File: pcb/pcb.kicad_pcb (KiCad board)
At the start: 2 copper layers, 152 x 91.6 mm, 66 parts, among them J1 USB_C_Receptacle_USB2.0_16P, J2 Conn_01x02, K1 SW_Push, K10 SW_Push, K11 SW_Push, K12 SW_Push, K13 SW_Push, K14 SW_Push, K15 SW_Push, K16 SW_Push, K17 SW_Push, K18 SW_Push, K19 SW_Push, K2 SW_Push, K20 SW_Push, K21 SW_Push, K3 SW_Push, K4 SW_Push, K5 SW_Push, K6 SW_Push, K7 SW_Push, K8 SW_Push, K9 SW_Push, U1 SRV05-4, U2 ProMicro, U3 SRV05-4

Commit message: cirrus40, second manufactured version
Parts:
- removed the D19 at (50.2, 74.3)
- removed the D20 at (63.5, 93.3)
- removed D22: DIODE, footprints:Diode-dual
- removed K19, K20, K21: SW_Push, footprints:SW_MX_HotSwap_Reversible
- removed the REF** at (97.5, 61.3)
- added C1: 470nF, Capacitor_SMD:C_0805_2012Metric_Pad1.18x1.45mm_HandSolder, B.Cu at (154.9, 94.0)
- added C3: 470nF, Capacitor_SMD:C_0805_2012Metric_Pad1.18x1.45mm_HandSolder, B.Cu at (159.4, 94.0)
- added D12: DIODE, footprints:Diode-dual, F.Cu at (158.1, 100.3)
- added D21: DIODE, footprints:Diode-dual, F.Cu at (160.7, 100.3)
- added R1: 10kOhm, Resistor_SMD:R_0805_2012Metric_Pad1.20x1.40mm_HandSolder, F.Cu at (155.6, 102.2)
- added R2: 10kOhm, Resistor_SMD:R_0805_2012Metric_Pad1.20x1.40mm_HandSolder, B.Cu at (155.6, 102.2)
- added R3: 8kOhm, Resistor_SMD:R_0805_2012Metric_Pad1.20x1.40mm_HandSolder, B.Cu at (155.6, 97.8)
- added R4: 8kOhm, Resistor_SMD:R_0805_2012Metric_Pad1.20x1.40mm_HandSolder, F.Cu at (155.6, 97.8)
- added R5: 10kOhm, Resistor_SMD:R_0805_2012Metric_Pad1.20x1.40mm_HandSolder, B.Cu at (163.2, 102.2)
- added R6: 10kOhm, Resistor_SMD:R_0805_2012Metric_Pad1.20x1.40mm_HandSolder, F.Cu at (163.2, 102.2)
- added R7: 8kOhm, Resistor_SMD:R_0805_2012Metric_Pad1.20x1.40mm_HandSolder, F.Cu at (163.2, 97.8)
- added R8: 8kOhm, Resistor_SMD:R_0805_2012Metric_Pad1.20x1.40mm_HandSolder, B.Cu at (163.2, 97.8)
- C2: renamed from C1; value 50V/100nF axial -> 470nF; footprint footprints:RESISTOR_Reversible -> Capacitor_SMD:C_0805_2012Metric_Pad1.18x1.45mm_HandSolder
- C4: renamed from C2; value 50V/100nF axial -> 470nF; footprint footprints:RESISTOR_Reversible -> Capacitor_SMD:C_0805_2012Metric_Pad1.18x1.45mm_HandSolder
- FB1: renamed from FB2; footprint footprints:C_0603_1608Metric_Pad1.08x0.95mm_HandSolder -> Capacitor_SMD:C_0805_2012Metric_Pad1.18x1.45mm_HandSolder
- FB2: renamed from FB3; footprint footprints:C_0603_1608Metric_Pad1.08x0.95mm_HandSolder -> Capacitor_SMD:C_0805_2012Metric_Pad1.18x1.45mm_HandSolder
- FB3: renamed from FB4; footprint footprints:C_0603_1608Metric_Pad1.08x0.95mm_HandSolder -> Capacitor_SMD:C_0805_2012Metric_Pad1.18x1.45mm_HandSolder
- FB4: renamed from FB1; footprint footprints:C_0603_1608Metric_Pad1.08x0.95mm_HandSolder -> Capacitor_SMD:C_0805_2012Metric_Pad1.18x1.45mm_HandSolder
- REF** (x6): value MountingHole_2.2mm_M2 -> MountingHole_3.5mm_TinyCourtyard; footprint MountingHole:MountingHole_2.2mm_M2 -> footprints:MountingHole_3.5mm_TinyCourtyard
- moved REF** 38.1 mm to (135.5, 102.2)
- moved J2 36.3 mm to (166.4, 64.1), turned to -90 degrees
- moved REF** 19.1 mm to (78.5, 65.9)
- moved REF** 19.1 mm to (78.5, 104.2)
- moved D14 17.4 mm to (125.5, 87.5)
- moved FB1 16.5 mm to (165.8, 110.3), turned to -90 degrees
- moved FB2 16.5 mm to (165.8, 110.3), turned to -90 degrees
- moved D2 15.3 mm to (68.6, 92.1)
- moved D10 15.3 mm to (106.5, 88.4)
- moved D5 15.0 mm to (87.6, 87.6)
- moved C2 13.2 mm to (154.9, 94.0), turned to 180 degrees
- moved FB3 12.2 mm to (163.5, 110.3), turned to -90 degrees
- moved FB4 12.2 mm to (163.5, 110.3), turned to -90 degrees
- moved D11 10.4 mm to (129.5, 118.7), turned to 90 degrees
- moved C4 8.63 mm to (159.4, 94.0), turned to 0 degrees
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- renumbered D13 to D1, D9 to D10, D18 to D11, D4 to D13, D5 to D14, D6 to D15, D17 to D16, D1 to D17, D2 to D18, D3 to D19, D14 to D2, D16 to D20, D15 to D3, D10 to D4, D11 to D5, D12 to D6, D21 to D7, D7 to D8, D8 to D9, K13 to K1, K18 to K10, K4 to K11, K5 to K12, K6 to K13, K17 to K14, K1 to K15, K2 to K16, K3 to K17, K16 to K18, K14 to K2, K15 to K3, K10 to K4, K11 to K5, K12 to K6, U3 to U1, U1 to U2, U2 to U3
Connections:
- C2 pad 1: ENCA -> ENCA_DB
- C4 pad 1: GND -> ENCB_DB
- C4 pad 2: ENCB -> GND
- U3 pad 2: ROW0 -> unconnected-(U3-GP2-Pad2)
- U3 pad 20: COL5 -> COL4
- U3 pad 22: COL4 -> COL3
- U3 pad 26: COL3 -> COL2
- U3 pad 27: COL2 -> COL1
- U3 pad 28: COL1 -> COL0
- U3 pad 29: COL0 -> unconnected-(U3-GP29-Pad29)
- U3 pad 3: ROW1 -> ROW0
- U3 pad 4: ROW2 -> ROW1
- U3 pad 5: ROW3 -> ROW2
- U3 pad 6: ENCA -> ROW3
- U3 pad 7: ENCB -> unconnected-(U3-GP7-Pad7)
- U3 pad 8: unconnected-(U2-GP8-Pad8)_1 -> ENCA_DB
- U3 pad 9: unconnected-(U2-GP9-Pad9) -> ENCB_DB
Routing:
- net COL5: track 202.3 -> 0.00 mm, vias 8 -> 0
- net ENCA: track 105.0 -> 58.5 mm, vias 6 -> 1
- net COL4: track 184.2 -> 142.7 mm, vias 6 -> 3
- net ENCB: track 95.8 -> 55.7 mm, vias 5 -> 1
- net /Batt: track 52.1 -> 12.2 mm, vias 2 -> 1
- net ROW1: track 143.1 -> 105.8 mm, vias 4 -> 2
- net ENCA_DB: track 0.00 -> 37.2 mm
- net COL0: track 176.6 -> 141.0 mm, vias 7 -> 4
- net ENCB_DB: track 0.00 -> 34.9 mm
- net Net-(D20-K) (its old number): track 32.6 -> 0.00 mm, vias 2 -> 0
- net ROW3: track 132.5 -> 102.9 mm, vias 3 -> 1
- net ROW2: track 127.8 -> 106.1 mm, vias 1 -> 2
- net ROW0: track 117.4 -> 96.4 mm, vias 0 -> 1
- net VCC: track 75.6 -> 96.4 mm, vias 8 -> 6
- net COL3: track 193.5 -> 174.3 mm, vias 7 -> 4
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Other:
- board size 152 x 91.6 mm -> 133.2 x 91.6 mm

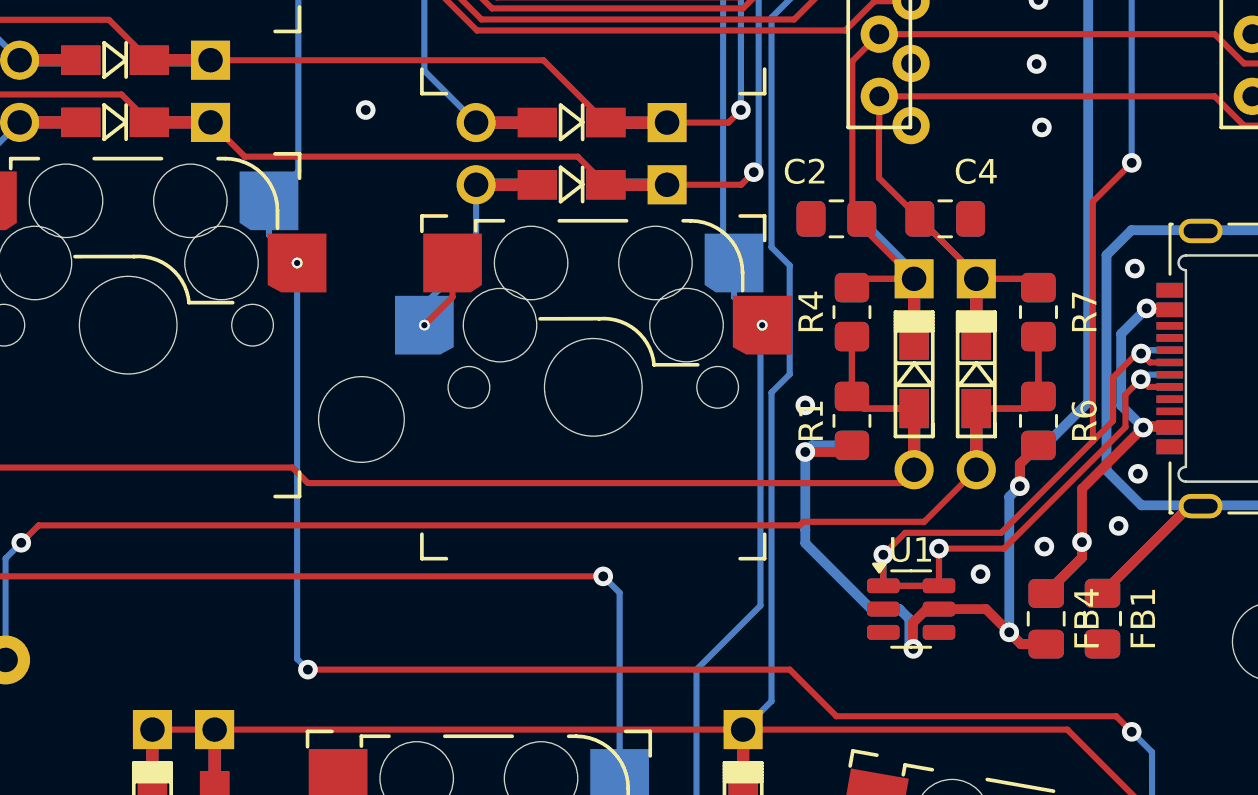
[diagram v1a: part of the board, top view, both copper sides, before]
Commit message: add cap/resistor labels and github link
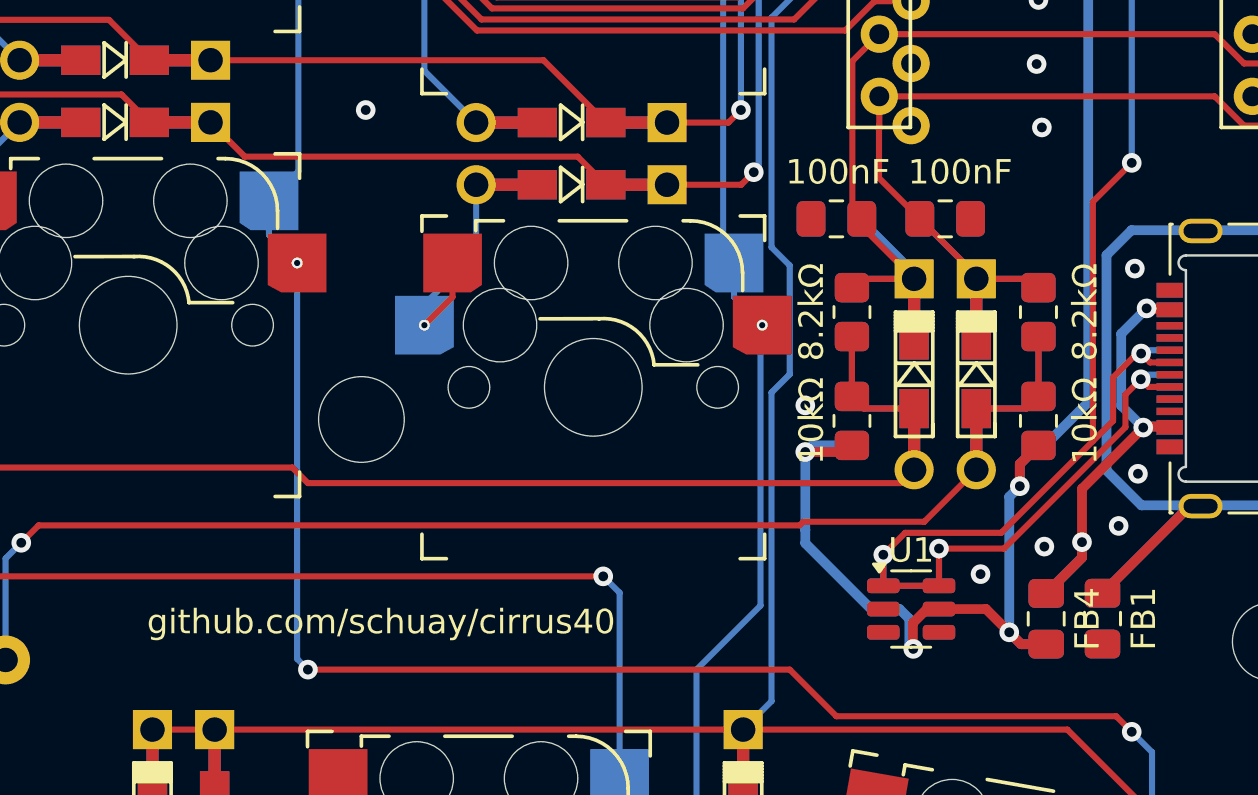
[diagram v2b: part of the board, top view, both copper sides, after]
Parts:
- renumbered C4 to 100nF, C2 to 100nF, C1 to 100nF, C3 to 100nF, R6 to 10kΩ, R1 to 10kΩ, R5 to 10kΩ, R2 to 10kΩ, R7 to 8.2kΩ, R4 to 8.2kΩ, R3 to 8.2kΩ, R8 to 8.2kΩ
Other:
- board text added: "github.com/schuay/cirrus40"
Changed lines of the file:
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@@
 		(descr "Capacitor SMD 0805 (2012 Metric), square (rectangular) end terminal, IPC-7351 nominal with elongated pad for handsoldering. (Body size source: IPC-SM-782 page 76, https://www.pcb-3d.com/wordpress/wp-content/uploads/ipc-sm-782a_amendment_1_and_2.pdf, https://docs.google.com/spreadsheets/d/1BsfQQcO9C6DZCsRaXUlFlo91Tg2WpOkGARC1WS5S8t0/edit?usp=sharing), generated with kicad-footprint-generator")
 		(tags "capacitor handsolder")
-		(property "Reference" "C4"
-			(at 1.27 -1.905 0)
+		(property "Reference" "100nF"
+			(at 0.615 -1.905 0)
 			(layer "F.SilkS")
 			(effects
@@
 		(descr "Resistor SMD 0805 (2012 Metric), square (rectangular) end terminal, IPC-7351 nominal with elongated pad for handsoldering. (Body size source: IPC-SM-782 page 72, https://www.pcb-3d.com/wordpress/wp-content/uploads/ipc-sm-782a_amendment_1_and_2.pdf), generated with kicad-footprint-generator")
 		(tags "resistor handsolder")
-		(property "Reference" "R6"
+		(property "Reference" "10kΩ"
 			(at 0 1.905 90)
 			(layer "F.SilkS")
@@
 		(descr "Resistor SMD 0805 (2012 Metric), square (rectangular) end terminal, IPC-7351 nominal with elongated pad for handsoldering. (Body size source: IPC-SM-782 page 72, https://www.pcb-3d.com/wordpress/wp-content/uploads/ipc-sm-782a_amendment_1_and_2.pdf), generated with kicad-footprint-generator")
 		(tags "resistor handsolder")
-		(property "Reference" "R1"
+		(property "Reference" "10kΩ"
 			(at 0 -1.65 90)
 			(layer "F.SilkS")
@@
 		(descr "Resistor SMD 0805 (2012 Metric), square (rectangular) end terminal, IPC-7351 nominal with elongated pad for handsoldering. (Body size source: IPC-SM-782 page 72, https://www.pcb-3d.com/wordpress/wp-content/uploads/ipc-sm-782a_amendment_1_and_2.pdf), generated with kicad-footprint-generator")
 		(tags "resistor handsolder")
-		(property "Reference" "R7"
+		(property "Reference" "8.2kΩ"
 			(at 0 1.905 90)
 			(layer "F.SilkS")
@@
 		(descr "Capacitor SMD 0805 (2012 Metric), square (rectangular) end terminal, IPC-7351 nominal with elongated pad for handsoldering. (Body size source: IPC-SM-782 page 76, https://www.pcb-3d.com/wordpress/wp-content/uploads/ipc-sm-782a_amendment_1_and_2.pdf, https://docs.google.com/spreadsheets/d/1BsfQQcO9C6DZCsRaXUlFlo91Tg2WpOkGARC1WS5S8t0/edit?usp=sharing), generated with kicad-footprint-generator")
 		(tags "capacitor handsolder")
-		(property "Reference" "C2"
-			(at 1.27 1.905 0)
+		(property "Reference" "100nF"
+			(at -0.06 1.905 0)
 			(layer "F.SilkS")
 			(effects
@@
 		(descr "Resistor SMD 0805 (2012 Metric), square (rectangular) end terminal, IPC-7351 nominal with elongated pad for handsoldering. (Body size source: IPC-SM-782 page 72, https://www.pcb-3d.com/wordpress/wp-content/uploads/ipc-sm-782a_amendment_1_and_2.pdf), generated with kicad-footprint-generator")
 		(tags "resistor handsolder")
-		(property "Reference" "R4"
+		(property "Reference" "8.2kΩ"
 			(at 0 -1.65 90)
 			(layer "F.SilkS")
@@
 		(descr "Resistor SMD 0805 (2012 Metric), square (rectangular) end terminal, IPC-7351 nominal with elongated pad for handsoldering. (Body size source: IPC-SM-782 page 72, https://www.pcb-3d.com/wordpress/wp-content/uploads/ipc-sm-782a_amendment_1_and_2.pdf), generated with kicad-footprint-generator")
 		(tags "resistor handsolder")
-		(property "Reference" "R5"
+		(property "Reference" "10kΩ"
 			(at 0 1.65 90)
 			(layer "B.SilkS")
@@
 		(descr "Capacitor SMD 0805 (2012 Metric), square (rectangular) end terminal, IPC-7351 nominal with elongated pad for handsoldering. (Body size source: IPC-SM-782 page 76, https://www.pcb-3d.com/wordpress/wp-content/uploads/ipc-sm-782a_amendment_1_and_2.pdf, https://docs.google.com/spreadsheets/d/1BsfQQcO9C6DZCsRaXUlFlo91Tg2WpOkGARC1WS5S8t0/edit?usp=sharing), generated with kicad-footprint-generator")
 		(tags "capacitor handsolder")
-		(property "Reference" "C1"
-			(at 1.27 1.905 0)
+		(property "Reference" "100nF"
+			(at -0.06 1.905 0)
 			(layer "B.SilkS")
 			(effects
@@
 		(descr "Resistor SMD 0805 (2012 Metric), square (rectangular) end terminal, IPC-7351 nominal with elongated pad for handsoldering. (Body size source: IPC-SM-782 page 72, https://www.pcb-3d.com/wordpress/wp-content/uploads/ipc-sm-782a_amendment_1_and_2.pdf), generated with kicad-footprint-generator")
 		(tags "resistor handsolder")
-		(property "Reference" "R3"
+		(property "Reference" "8.2kΩ"
 			(at 0 -1.905 90)
 			(layer "B.SilkS")
@@
 		(descr "Resistor SMD 0805 (2012 Metric), square (rectangular) end terminal, IPC-7351 nominal with elongated pad for handsoldering. (Body size source: IPC-SM-782 page 72, https://www.pcb-3d.com/wordpress/wp-content/uploads/ipc-sm-782a_amendment_1_and_2.pdf), generated with kicad-footprint-generator")
 		(tags "resistor handsolder")
-		(property "Reference" "R2"
+		(property "Reference" "10kΩ"
 			(at 0 -1.905 90)
 			(layer "B.SilkS")
@@
 		(descr "Capacitor SMD 0805 (2012 Metric), square (rectangular) end terminal, IPC-7351 nominal with elongated pad for handsoldering. (Body size source: IPC-SM-782 page 76, https://www.pcb-3d.com/wordpress/wp-content/uploads/ipc-sm-782a_amendment_1_and_2.pdf, https://docs.google.com/spreadsheets/d/1BsfQQcO9C6DZCsRaXUlFlo91Tg2WpOkGARC1WS5S8t0/edit?usp=sharing), generated with kicad-footprint-generator")
 		(tags "capacitor handsolder")
-		(property "Reference" "C3"
-			(at 1.27 -1.905 0)
+		(property "Reference" "100nF"
+			(at 0.615 -1.905 0)
 			(layer "B.SilkS")
 			(effects
@@
 		(descr "Resistor SMD 0805 (2012 Metric), square (rectangular) end terminal, IPC-7351 nominal with elongated pad for handsoldering. (Body size source: IPC-SM-782 page 72, https://www.pcb-3d.com/wordpress/wp-content/uploads/ipc-sm-782a_amendment_1_and_2.pdf), generated with kicad-footprint-generator")
 		(tags "resistor handsolder")
-		(property "Reference" "R8"
+		(property "Reference" "8.2kΩ"
 			(at 0 1.65 90)
 			(layer "B.SilkS")
@@
 		(layer "Edge.Cuts")
 	)
+	(gr_text "github.com/schuay/cirrus40"
+		(at 126.771853 111.032295 0)
+		(layer "F.SilkS")
+		(effects
+			(font
+				(size 1 1)
+				(thickness 0.15)
+			)
+			(justify left bottom)
+		)
+	)
+	(gr_text "github.com/schuay/cirrus40"
+		(at 168.263474 90.461898 270)
+		(layer "B.SilkS")
+		(effects
+			(font
+				(size 1 1)
+				(thickness 0.15)
+			)
+			(justify left bottom mirror)
+		)
+	)
 	(segment
